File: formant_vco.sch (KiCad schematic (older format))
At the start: 80 parts, among them J1 JACK_2P, J2 JACK_2P, J3 JACK_2P, J4 CONN_02X08, J5 JACK_2P, Q1 BC850, Q2 BC850, Q3 BC850, Q4 BC850, Q5 BC850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

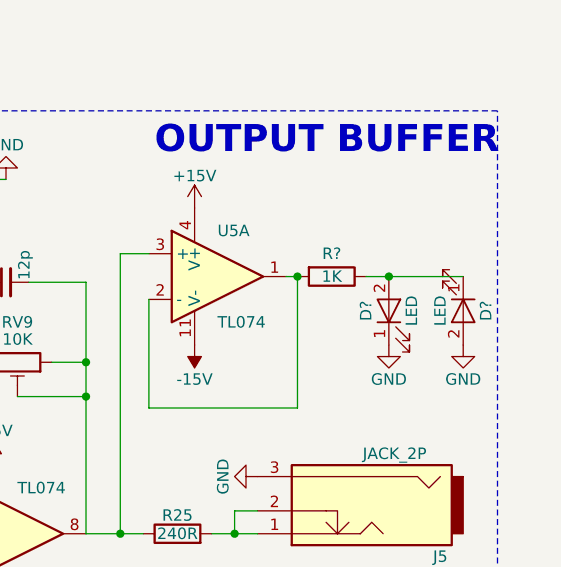
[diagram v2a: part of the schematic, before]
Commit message: Add footprints for mono jack and alpha pots
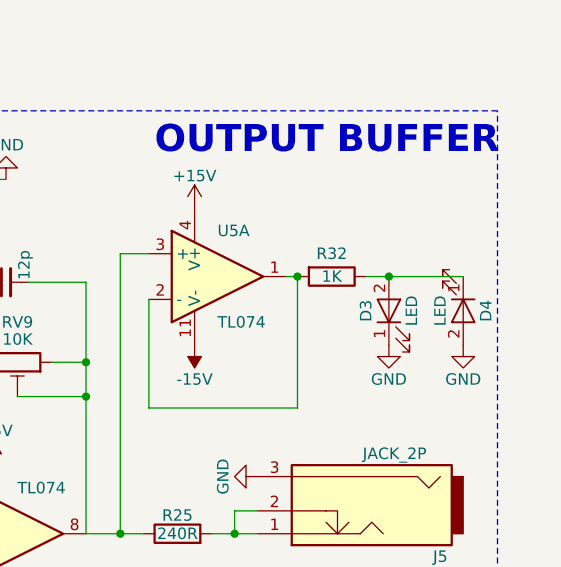
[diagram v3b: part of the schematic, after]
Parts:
- C1, C12, C13, C15, C16, C2, C4: footprint Capacitors_Tantalum_SMD:CP_Tantalum_Case-A_EIA-3216-18_Hand -> Capacitors_Tantalum_SMD:CP_Tantalum_Case-A_EIA-3216-18_Reflow
- D3, D4: renamed from D?; footprint (none) -> LEDs:LED_D5.0mm
- J1, J2, J3: footprint Pin_Headers:Pin_Header_Straight_1x03_Pitch2.54mm -> footprint_pj3010bm:pj301bm
- J4: footprint (none) -> Connectors:IDC_Header_Straight_16pins
- J5: footprint Socket_Strips:Socket_Strip_Straight_1x03_Pitch2.54mm -> footprint_pj3010bm:pj301bm
- RV1, RV2, RV3, RV4: footprint Potentiometers:Potentiometer_Bourns_PTV09A-1_Horizontal -> footprint_alpha_d_pot:alpha_d_pot_vert
- gave numbers to parts that had none: 1
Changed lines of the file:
@@
 F 0 "C1" H 710 1070 50  0000 L CNN
 F 1 "1u" H 710 920 50  0000 L CNN
-F 2 "Capacitors_Tantalum_SMD:CP_Tantalum_Case-A_EIA-3216-18_Hand" H 700 1000 50  0001 C CNN
+F 2 "Capacitors_Tantalum_SMD:CP_Tantalum_Case-A_EIA-3216-18_Reflow" H 700 1000 50  0001 C CNN
 F 3 "" H 700 1000 50  0001 C CNN
 	1    700  1000
@@
 F 0 "C2" H 2210 870 50  0000 L CNN
 F 1 "1u" H 2210 720 50  0000 L CNN
-F 2 "Capacitors_Tantalum_SMD:CP_Tantalum_Case-A_EIA-3216-18_Hand" H 2200 800 50  0001 C CNN
+F 2 "Capacitors_Tantalum_SMD:CP_Tantalum_Case-A_EIA-3216-18_Reflow" H 2200 800 50  0001 C CNN
 F 3 "" H 2200 800 50  0001 C CNN
 	1    2200 800
@@
 F 0 "RV1" V 1475 2400 50  0000 C CNN
 F 1 "10K LIN" V 1550 2400 50  0000 C CNN
-F 2 "Potentiometers:Potentiometer_Bourns_PTV09A-1_Horizontal" H 1650 2400 50  0001 C CNN
+F 2 "footprint_alpha_d_pot:alpha_d_pot_vert" H 1650 2400 50  0001 C CNN
 F 3 "" H 1650 2400 50  0001 C CNN
 	1    1650 2400
@@
 F 0 "RV2" V 1475 2950 50  0000 C CNN
 F 1 "100K LIN" V 1550 2950 50  0000 C CNN
-F 2 "Potentiometers:Potentiometer_Bourns_PTV09A-1_Horizontal" H 1650 2950 50  0001 C CNN
+F 2 "footprint_alpha_d_pot:alpha_d_pot_vert" H 1650 2950 50  0001 C CNN
 F 3 "" H 1650 2950 50  0001 C CNN
 	1    1650 2950
@@
 F 0 "J1" H 800 3850 50  0000 C CNN
 F 1 "JACK_2P" H 1000 4300 50  0000 C CNN
-F 2 "Pin_Headers:Pin_Header_Straight_1x03_Pitch2.54mm" H 1150 4050 50  0001 C CNN
+F 2 "footprint_pj3010bm:pj301bm" H 1150 4050 50  0001 C CNN
 F 3 "" H 1150 4050 50  0001 C CNN
 	1    1150 4050
@@
 F 0 "J2" H 800 4350 50  0000 C CNN
 F 1 "JACK_2P" H 1000 4800 50  0000 C CNN
-F 2 "Pin_Headers:Pin_Header_Straight_1x03_Pitch2.54mm" H 1150 4550 50  0001 C CNN
+F 2 "footprint_pj3010bm:pj301bm" H 1150 4550 50  0001 C CNN
 F 3 "" H 1150 4550 50  0001 C CNN
 	1    1150 4550
@@
 F 0 "RV3" V 1625 4800 50  0000 C CNN
 F 1 "100K LIN" V 1700 4800 50  0000 C CNN
-F 2 "Potentiometers:Potentiometer_Bourns_PTV09A-1_Horizontal" H 1800 4800 50  0001 C CNN
+F 2 "footprint_alpha_d_pot:alpha_d_pot_vert" H 1800 4800 50  0001 C CNN
 F 3 "" H 1800 4800 50  0001 C CNN
 	1    1800 4800
@@
 F 0 "J3" H 1125 6475 50  0000 C CNN
 F 1 "JACK_2P" H 1325 6925 50  0000 C CNN
-F 2 "Pin_Headers:Pin_Header_Straight_1x03_Pitch2.54mm" H 1475 6675 50  0001 C CNN
+F 2 "footprint_pj3010bm:pj301bm" H 1475 6675 50  0001 C CNN
 F 3 "" H 1475 6675 50  0001 C CNN
 	1    1475 6675
@@
 F 0 "RV4" V 2150 6775 50  0000 C CNN
 F 1 "100K LIN" V 2225 6775 50  0000 C CNN
-F 2 "Potentiometers:Potentiometer_Bourns_PTV09A-1_Horizontal" H 2325 6775 50  0001 C CNN
+F 2 "footprint_alpha_d_pot:alpha_d_pot_vert" H 2325 6775 50  0001 C CNN
 F 3 "" H 2325 6775 50  0001 C CNN
 	1    2325 6775
@@
 F 0 "J5" H 10050 2750 50  0000 C CNN
 F 1 "JACK_2P" H 10250 3200 50  0000 C CNN
-F 2 "Socket_Strips:Socket_Strip_Straight_1x03_Pitch2.54mm" H 10400 2950 50  0001 C CNN
+F 2 "footprint_pj3010bm:pj301bm" H 10400 2950 50  0001 C CNN
 F 3 "" H 10400 2950 50  0001 C CNN
 	1    10400 2950
@@
 F 0 "C4" H 6085 1095 50  0000 L CNN
 F 1 "100u" H 6085 945 50  0000 L CNN
-F 2 "Capacitors_Tantalum_SMD:CP_Tantalum_Case-A_EIA-3216-18_Hand" H 6075 1025 50  0001 C CNN
+F 2 "Capacitors_Tantalum_SMD:CP_Tantalum_Case-A_EIA-3216-18_Reflow" H 6075 1025 50  0001 C CNN
 F 3 "" H 6075 1025 50  0001 C CNN
 	1    6075 1025
@@
 $EndComp
 $Comp
-L -15V #PWR52
+L -15V #PWR54
 U 1 1 59626FF8
 P 10100 6000
-F 0 "#PWR52" H 10100 6100 50  0001 C CNN
+F 0 "#PWR54" H 10100 6100 50  0001 C CNN
 F 1 "-15V" H 10100 6150 50  0000 C CNN
 F 2 "" H 10100 6000 50  0001 C CNN
@@
 F 0 "C12" H 7510 970 50  0000 L CNN
 F 1 "10u" V 7400 800 50  0000 L CNN
-F 2 "Capacitors_Tantalum_SMD:CP_Tantalum_Case-A_EIA-3216-18_Hand" H 7500 900 50  0001 C CNN
+F 2 "Capacitors_Tantalum_SMD:CP_Tantalum_Case-A_EIA-3216-18_Reflow" H 7500 900 50  0001 C CNN
 F 3 "" H 7500 900 50  0001 C CNN
 	1    7500 900
@@
 F 0 "C13" H 7510 1170 50  0000 L CNN
 F 1 "10u" V 7400 1000 50  0000 L CNN
-F 2 "Capacitors_Tantalum_SMD:CP_Tantalum_Case-A_EIA-3216-18_Hand" H 7500 1100 50  0001 C CNN
+F 2 "Capacitors_Tantalum_SMD:CP_Tantalum_Case-A_EIA-3216-18_Reflow" H 7500 1100 50  0001 C CNN
 F 3 "" H 7500 1100 50  0001 C CNN
 	1    7500 1100
@@
 F 0 "C15" H 7760 970 50  0000 L CNN
 F 1 "10u" V 7650 800 50  0000 L CNN
-F 2 "Capacitors_Tantalum_SMD:CP_Tantalum_Case-A_EIA-3216-18_Hand" H 7750 900 50  0001 C CNN
+F 2 "Capacitors_Tantalum_SMD:CP_Tantalum_Case-A_EIA-3216-18_Reflow" H 7750 900 50  0001 C CNN
 F 3 "" H 7750 900 50  0001 C CNN
 	1    7750 900
@@
 F 0 "C16" H 7760 1170 50  0000 L CNN
 F 1 "10u" V 7650 1000 50  0000 L CNN
-F 2 "Capacitors_Tantalum_SMD:CP_Tantalum_Case-A_EIA-3216-18_Hand" H 7750 1100 50  0001 C CNN
+F 2 "Capacitors_Tantalum_SMD:CP_Tantalum_Case-A_EIA-3216-18_Reflow" H 7750 1100 50  0001 C CNN
 F 3 "" H 7750 1100 50  0001 C CNN
 	1    7750 1100
@@
 F 0 "J4" H 4825 1425 50  0000 C CNN
 F 1 "CONN_02X08" V 4825 975 50  0000 C CNN
-F 2 "" H 4825 -225 50  0001 C CNN
+F 2 "Connectors:IDC_Header_Straight_16pins" H 4825 -225 50  0001 C CNN
 F 3 "" H 4825 -225 50  0001 C CNN
 	1    4825 975
@@
 $EndComp
 $Comp
-L -15V #PWR?
+L -15V #PWR51
 U 1 1 5969C174
 P 9675 2225
-F 0 "#PWR?" H 9675 2325 50  0001 C CNN
+F 0 "#PWR51" H 9675 2325 50  0001 C CNN
 F 1 "-15V" H 9675 2375 50  0000 C CNN
 F 2 "" H 9675 2225 50  0001 C CNN
@@
 $EndComp
 $Comp
-L +15V #PWR?
+L +15V #PWR043
 U 1 1 5969C4B0
 P 9675 1625
-F 0 "#PWR?" H 9675 1475 50  0001 C CNN
+F 0 "#PWR043" H 9675 1475 50  0001 C CNN
 F 1 "+15V" H 9675 1765 50  0000 C CNN
 F 2 "" H 9675 1625 50  0001 C CNN
@@
 Connection ~ 9350 3050
 $Comp
-L R R?
+L R R32
 U 1 1 5969C9D5
 P 10275 1925
-F 0 "R?" V 10175 1925 50  0000 C CNN
+F 0 "R32" V 10175 1925 50  0000 C CNN
 F 1 "1K" V 10275 1925 50  0000 C CNN
 F 2 "Resistors_SMD:R_0603" V 10205 1925 50  0001 C CNN
@@
 Connection ~ 10125 1925
 $Comp
-L LED D?
+L LED D3
 U 1 1 5969DEA1
 P 10525 2075
-F 0 "D?" H 10525 2175 50  0000 C CNN
+F 0 "D3" H 10525 2175 50  0000 C CNN
 F 1 "LED" H 10525 1975 50  0000 C CNN
-F 2 "" H 10525 2075 50  0001 C CNN
+F 2 "LEDs:LED_D5.0mm" H 10525 2075 50  0001 C CNN
 F 3 "" H 10525 2075 50  0001 C CNN
 	1    10525 2075
@@
 $EndComp
 $Comp
-L GND #PWR?
+L GND #PWR044
 U 1 1 5969E2E1
 P 10525 2225
-F 0 "#PWR?" H 10525 1975 50  0001 C CNN
+F 0 "#PWR044" H 10525 1975 50  0001 C CNN
 F 1 "GND" H 10525 2075 50  0000 C CNN
 F 2 "" H 10525 2225 50  0001 C CNN
@@
 	10425 1925 10850 1925
 $Comp
-L LED D?
+L LED D4
 U 1 1 596A27BF
 P 10850 2075
-F 0 "D?" H 10850 2175 50  0000 C CNN
+F 0 "D4" H 10850 2175 50  0000 C CNN
 F 1 "LED" H 10850 1975 50  0000 C CNN
-F 2 "" H 10850 2075 50  0001 C CNN
+F 2 "LEDs:LED_D5.0mm" H 10850 2075 50  0001 C CNN
 F 3 "" H 10850 2075 50  0001 C CNN
 	1    10850 2075
@@
 $EndComp
 $Comp
-L GND #PWR?
+L GND #PWR045
 U 1 1 596A2901
 P 10850 2225
-F 0 "#PWR?" H 10850 1975 50  0001 C CNN
+F 0 "#PWR045" H 10850 1975 50  0001 C CNN
 F 1 "GND" H 10850 2075 50  0000 C CNN
 F 2 "" H 10850 2225 50  0001 C CNN

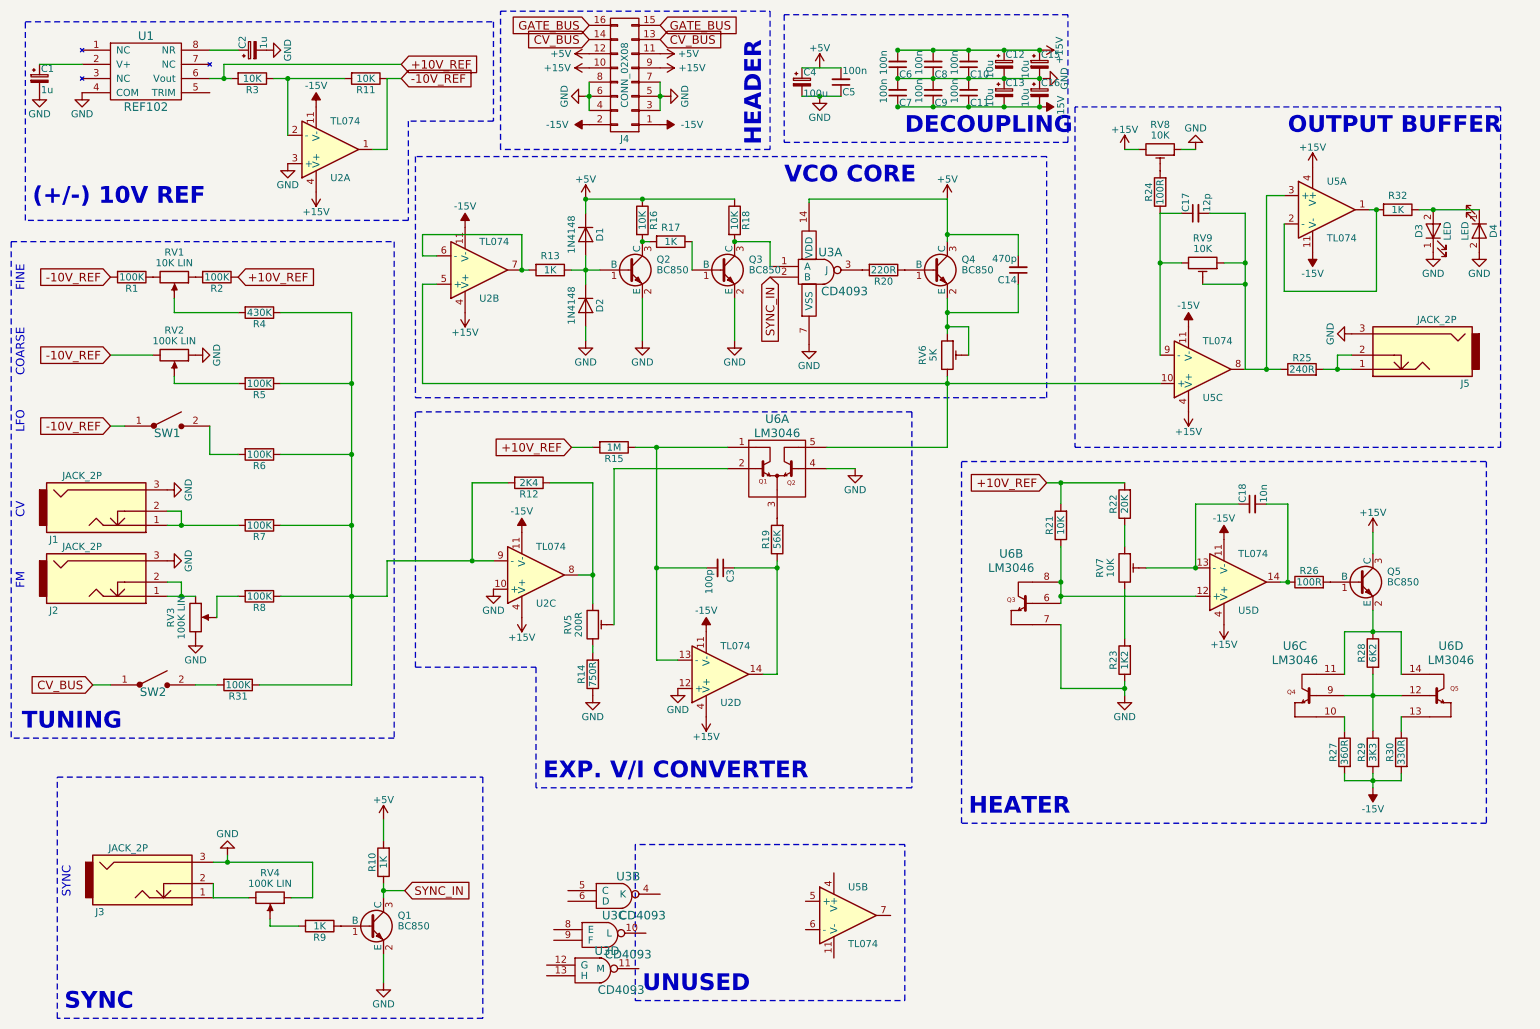
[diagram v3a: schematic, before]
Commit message: Swap TL074 for TL072
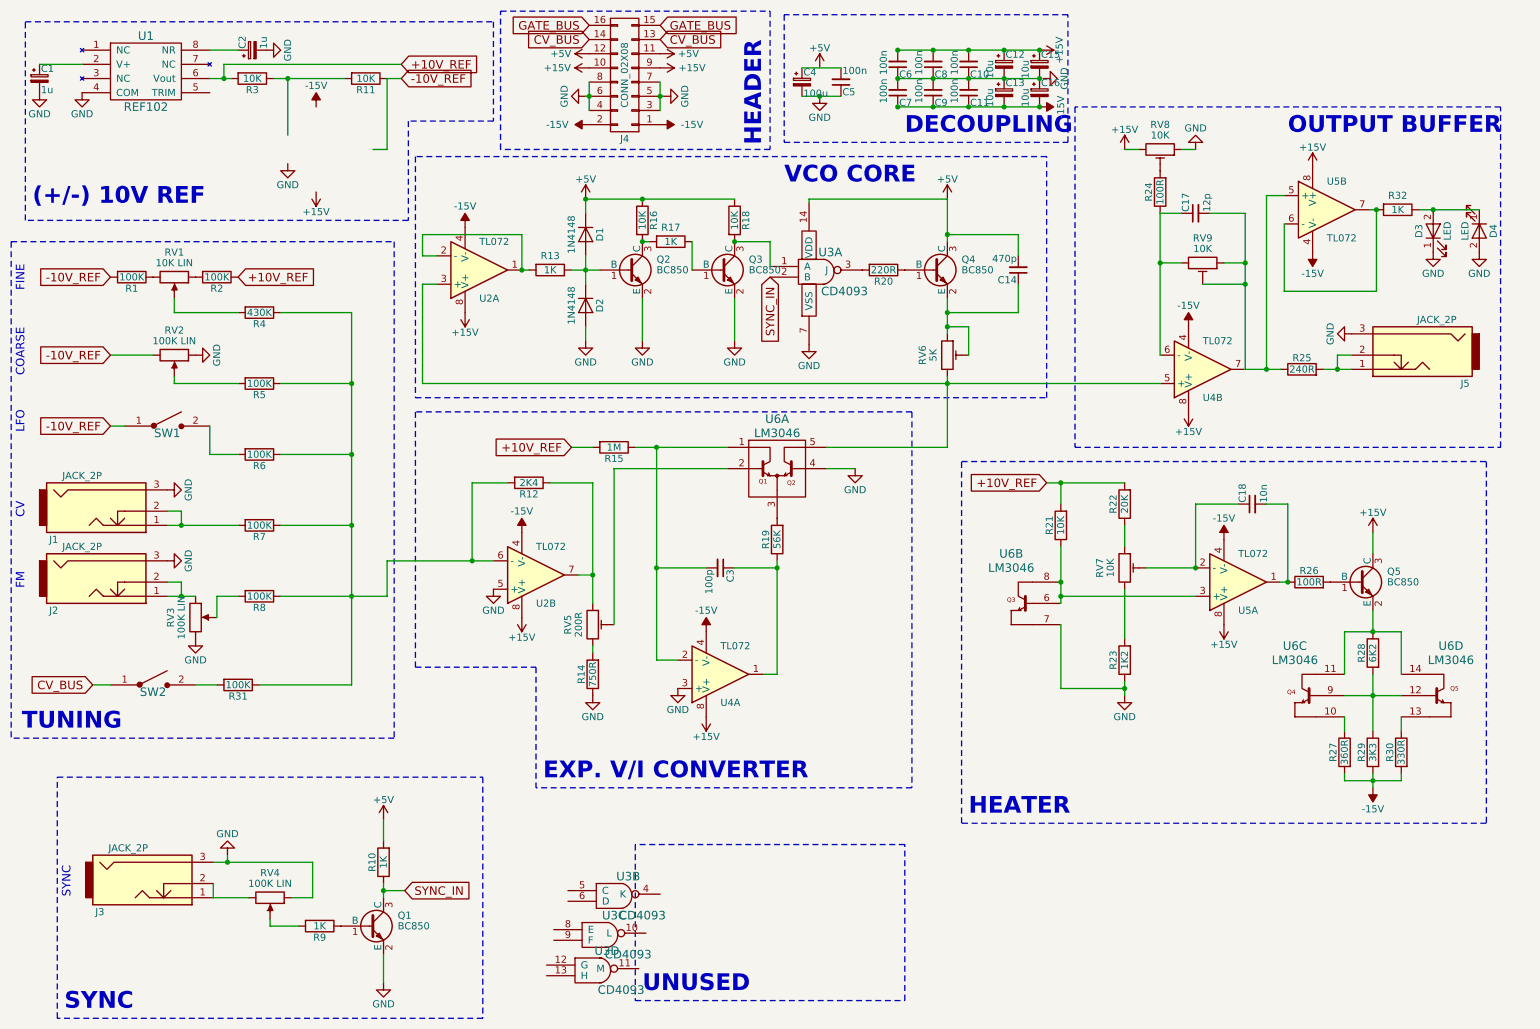
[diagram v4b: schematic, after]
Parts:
- removed U2, U5: TL074, Housings_SOIC:SOIC-14_3.9x8.7mm_Pitch1.27mm, symbol TL074
- added U2, U4, U5: TL072, Housings_SOIC:SOIC-8_3.9x4.9mm_Pitch1.27mm, symbol TL072
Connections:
- net +15V: now also U2.8 (V+), U2.8 (V+), U4.8 (V+), U4.8 (V+), U5.8 (V+), U5.8 (V+)
- net -15V: now also U2.4 (V-), U2.4 (V-), U4.4 (V-), U4.4 (V-), U5.4 (V-), U5.4 (V-)
- net GND: now also U2.5 (+), U4.3 (+)
- net at R12.1, RV5.1: now also U2.7
- net at R12.2, R31.1, R4.1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: now also U2.6 (-)
- net at RV6.3, U6.5: now also U2.3 (+), U4.5 (+)
- net at R13.2: now also U2.1, U2.2 (-)
- net at C3.2, R15.1, U6.1: now also U4.2 (-)
- net at C3.1, R19.1: now also U4.1
- net at C18.1, RV7.2: now also U5.2 (-)
- net at C18.2, R26.1: now also U5.1
- net at R21.1, U6.6, U6.8: now also U5.3 (+)
- net at C17.1, R24.1, RV9.3: now also U4.6 (-)
- net at C17.2, R25.1, RV9.1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: now also U4.7, U5.5 (+)
- net at R32.2: now also U5.6 (-), U5.7
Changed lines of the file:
@@
 $EndDescr
-$Comp
-L TL074 U2
-U 1 1 59601B51
-P 2750 1500
-F 0 "U2" H 2750 1700 50  0000 L CNN
-F 1 "TL074" H 2750 1300 50  0000 L CNN
-F 2 "Housings_SOIC:SOIC-14_3.9x8.7mm_Pitch1.27mm" H 2700 1600 50  0001 C CNN
-F 3 "" H 2800 1700 50  0001 C CNN
-	1    2750 1500
-	1    0    0    1
-$EndComp
-$Comp
-L TL074 U2
-U 3 1 59601BD9
-P 4200 4500
-F 0 "U2" H 4200 4700 50  0000 L CNN
-F 1 "TL074" H 4200 4300 50  0000 L CNN
-F 2 "Housings_SOIC:SOIC-14_3.9x8.7mm_Pitch1.27mm" H 4150 4600 50  0001 C CNN
-F 3 "" H 4250 4700 50  0001 C CNN
-	3    4200 4500
-	1    0    0    1
-$EndComp
-$Comp
-L TL074 U2
-U 2 1 59601C2E
-P 3800 2350
-F 0 "U2" H 3800 2550 50  0000 L CNN
-F 1 "TL074" H 3800 2150 50  0000 L CNN
-F 2 "Housings_SOIC:SOIC-14_3.9x8.7mm_Pitch1.27mm" H 3750 2450 50  0001 C CNN
-F 3 "" H 3850 2550 50  0001 C CNN
-	2    3800 2350
-	1    0    0    1
-$EndComp
 $Comp
 L +15V #PWR01
@@
 $EndComp
 $Comp
-L TL074 U2
-U 4 1 5960790D
-P 5500 5200
-F 0 "U2" H 5500 5400 50  0000 L CNN
-F 1 "TL074" H 5500 5000 50  0000 L CNN
-F 2 "Housings_SOIC:SOIC-14_3.9x8.7mm_Pitch1.27mm" H 5450 5300 50  0001 C CNN
-F 3 "" H 5550 5400 50  0001 C CNN
-	4    5500 5200
-	1    0    0    1
-$EndComp
-$Comp
 L +15V #PWR013
 U 1 1 59607DCA
@@
 	1    8900 2300
 	0    1    1    0
-$EndComp
-$Comp
-L TL074 U5
-U 3 1 59630A92
-P 8900 3050
-F 0 "U5" H 8900 3250 50  0000 L CNN
-F 1 "TL074" H 8900 2850 50  0000 L CNN
-F 2 "Housings_SOIC:SOIC-14_3.9x8.7mm_Pitch1.27mm" H 8850 3150 50  0001 C CNN
-F 3 "" H 8950 3250 50  0001 C CNN
-	3    8900 3050
-	1    0    0    1
-$EndComp
-$Comp
-L TL074 U5
-U 1 1 59630B3B
-P 9775 1925
-F 0 "U5" H 9775 2125 50  0000 L CNN
-F 1 "TL074" H 9775 1725 50  0000 L CNN
-F 2 "Housings_SOIC:SOIC-14_3.9x8.7mm_Pitch1.27mm" H 9725 2025 50  0001 C CNN
-F 3 "" H 9825 2125 50  0001 C CNN
-	1    9775 1925
-	1    0    0    -1
-$EndComp
-$Comp
-L TL074 U5
-U 4 1 59630C28
-P 9150 4550
-F 0 "U5" H 9150 4750 50  0000 L CNN
-F 1 "TL074" H 9150 4350 50  0000 L CNN
-F 2 "Housings_SOIC:SOIC-14_3.9x8.7mm_Pitch1.27mm" H 9100 4650 50  0001 C CNN
-F 3 "" H 9200 4750 50  0001 C CNN
-	4    9150 4550
-	1    0    0    1
-$EndComp
-$Comp
-L TL074 U5
-U 2 1 59630CC3
-P 6400 6900
-F 0 "U5" H 6400 7100 50  0000 L CNN
-F 1 "TL074" H 6400 6700 50  0000 L CNN
-F 2 "Housings_SOIC:SOIC-14_3.9x8.7mm_Pitch1.27mm" H 6350 7000 50  0001 C CNN
-F 3 "" H 6450 7100 50  0001 C CNN
-	2    6400 6900
-	1    0    0    -1
 $EndComp
 $Comp
@@
 Wire Wire Line
 	9475 1825 9350 1825
+$Comp
+L TL072 U2
+U 2 1 596B241F
+P 4200 4500
+F 0 "U2" H 4200 4700 50  0000 L CNN
+F 1 "TL072" H 4200 4300 50  0000 L CNN
+F 2 "Housings_SOIC:SOIC-8_3.9x4.9mm_Pitch1.27mm" H 4200 4500 50  0001 C CNN
+F 3 "" H 4200 4500 50  0001 C CNN
+	2    4200 4500
+	1    0    0    1
+$EndComp
+$Comp
+L TL072 U4
+U 1 1 596B2732
+P 5500 5200
+F 0 "U4" H 5500 5400 50  0000 L CNN
+F 1 "TL072" H 5500 5000 50  0000 L CNN
+F 2 "Housings_SOIC:SOIC-8_3.9x4.9mm_Pitch1.27mm" H 5500 5200 50  0001 C CNN
+F 3 "" H 5500 5200 50  0001 C CNN
+	1    5500 5200
+	1    0    0    1
+$EndComp
+$Comp
+L TL072 U5
+U 1 1 596B288E
+P 9150 4550
+F 0 "U5" H 9150 4750 50  0000 L CNN
+F 1 "TL072" H 9150 4350 50  0000 L CNN
+F 2 "Housings_SOIC:SOIC-8_3.9x4.9mm_Pitch1.27mm" H 9150 4550 50  0001 C CNN
+F 3 "" H 9150 4550 50  0001 C CNN
+	1    9150 4550
+	1    0    0    1
+$EndComp
+$Comp
+L TL072 U4
+U 2 1 596B30CA
+P 8900 3050
+F 0 "U4" H 8900 3250 50  0000 L CNN
+F 1 "TL072" H 8900 2850 50  0000 L CNN
+F 2 "Housings_SOIC:SOIC-8_3.9x4.9mm_Pitch1.27mm" H 8900 3050 50  0001 C CNN
+F 3 "" H 8900 3050 50  0001 C CNN
+	2    8900 3050
+	1    0    0    1
+$EndComp
+$Comp
+L TL072 U2
+U 1 1 596B34D6
+P 3800 2350
+F 0 "U2" H 3800 2550 50  0000 L CNN
+F 1 "TL072" H 3800 2150 50  0000 L CNN
+F 2 "Housings_SOIC:SOIC-8_3.9x4.9mm_Pitch1.27mm" H 3800 2350 50  0001 C CNN
+F 3 "" H 3800 2350 50  0001 C CNN
+	1    3800 2350
+	1    0    0    1
+$EndComp
+$Comp
+L TL072 U5
+U 2 1 596B443D
+P 9775 1925
+F 0 "U5" H 9775 2125 50  0000 L CNN
+F 1 "TL072" H 9775 1725 50  0000 L CNN
+F 2 "Housings_SOIC:SOIC-8_3.9x4.9mm_Pitch1.27mm" H 9775 1925 50  0001 C CNN
+F 3 "" H 9775 1925 50  0001 C CNN
+	2    9775 1925
+	1    0    0    -1
+$EndComp
 $EndSCHEMATC
